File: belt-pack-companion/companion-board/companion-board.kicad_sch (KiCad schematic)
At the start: 4 parts, among them J1 Conn_01x18_Socket, J2 Conn_01x18_Socket, J3 AudioJack4_Ground, U1 TLV320AIC3204

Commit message: companion board update
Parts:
- added D1: Red, PCM_JLCPCB:D_0603, symbol PCM_JLCPCB-Diodes:LED,0603,Red
- added D2: White, PCM_JLCPCB:D_0603, symbol PCM_JLCPCB-Diodes:LED,0603,White
- added D3: Yellow, PCM_JLCPCB:D_0603, symbol PCM_JLCPCB-Diodes:LED,0603,Yellow
- added D4: Green, PCM_JLCPCB:D_0805, symbol PCM_JLCPCB-Diodes:LED,0805,Green
- added J4: Micro_SD_Card, symbol Connector:Micro_SD_Card
- added R1, R2, R3, R4: 27Ω, PCM_JLCPCB:R_0603, symbol PCM_JLCPCB-Resistors:0603,27Ω
- added R5: 10Ω, PCM_JLCPCB:R_0603, symbol PCM_JLCPCB-Resistors:0603,10Ω
- added S1, S2: Tactile Button, 160gf, PCM_JLCPCB:SW_TS-1088-AR02016, symbol PCM_JLCPCB-Connectors_Buttons:Tactile Button, 160gf, 12V, 50mA, 4.0mm
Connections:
- net GND: now reaches J2.1 (Pin_1)
- net GND: now also J1.1 (Pin_1), U1.12 (SPI_SELECT), U1.17 (AVSS), U1.28 (DVSS), U1.33 (EP), U1.7 (IOVSS)
- net +5V: now reaches J2.2 (Pin_2)
- net at U1.1 (MCLK): now also R5.2
- net I^{2}C_SDA: now reaches U1.10 (SDA/MOSI)
- net I^{2}C_SDA: now also J1.16 (Pin_16)
- net at U1.2 (BCLK): now also R3.2
- net at U1.3 (WCLK): now also R4.2
- net at U1.4 (DIN/MFP1): now also R1.2
- net at U1.5 (DOUT/MFP2): now also R2.2
- net I^{2}C_SCL: now reaches U1.9 (SCL/~{SS})
- net I^{2}C_SCL: now also J1.17 (Pin_17)
- net I^{2}S_BCLK: now reaches J1.12 (Pin_12)
- net I^{2}S_BCLK: now also R4.1
- net I^{2}S_WCLK: now reaches J1.13 (Pin_13)
- net I^{2}S_WCLK: now also R3.1
- net I^{2}S_MIC_DATA: now reaches J1.14 (Pin_14)
- net I^{2}S_MIC_DATA: now also R2.1
- net I^{2}S_SPK_DATA: now reaches J1.15 (Pin_15)
- net I^{2}S_SPK_DATA: now also R1.1
- net +3.3V: now reaches J1.2 (Pin_2)
- net +3.3V: now also J1.3 (Pin_3)
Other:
- note added: "Heltec LoRa V3"
- note added: "USB-C"
- moved on the sheet: J1, J2, J3, U1

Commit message: companion-board schematic update
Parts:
- added C1, C4: 10uF, PCM_JLCPCB:C_0402, symbol PCM_JLCPCB-Capacitors:0402,10uF
- added C2: 1uF, PCM_JLCPCB:C_0402, symbol PCM_JLCPCB-Capacitors:0402,1uF
- added C3: 1nF, PCM_JLCPCB:C_0402, symbol PCM_JLCPCB-Capacitors:0402,1nF
- added C5, C6: 47uF, PCM_JLCPCB:C_0805, symbol PCM_JLCPCB-Capacitors:0805,47uF
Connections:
- net +3.3V: now also U1.26 (LDOIN/HPVDD), U1.30 (LDO_SELECT), C1.1, C2.1, C3.1
- net GND: now also J3.G, C1.2, C2.2, C3.2, C4.2
- net at U1.18 (REF): now also C4.1
- net at U1.25 (HPL): now also C5.1
- net at U1.27 (HPR): now also C6.1
- net CODEC_RESET: now reaches U1.31 (~{RESET})
- net CODEC_RESET: now also J1.6 (Pin_6)
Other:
- moved on the sheet: J3, R1, R2, R3, R4, R5, U1

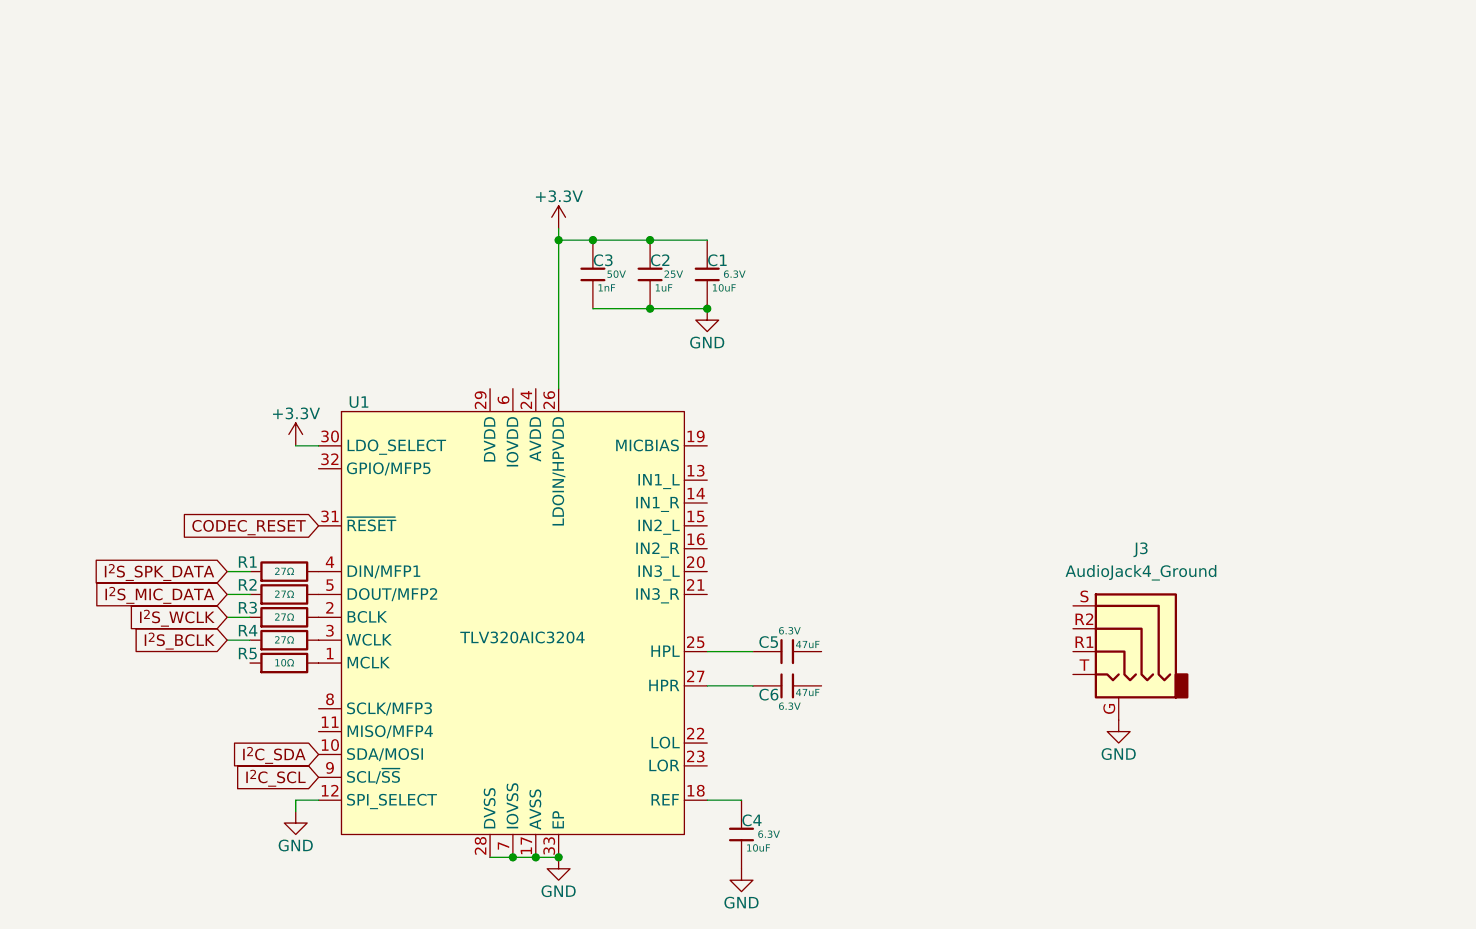
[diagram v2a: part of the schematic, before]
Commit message: Added connections to TRRS jack and some capacitors
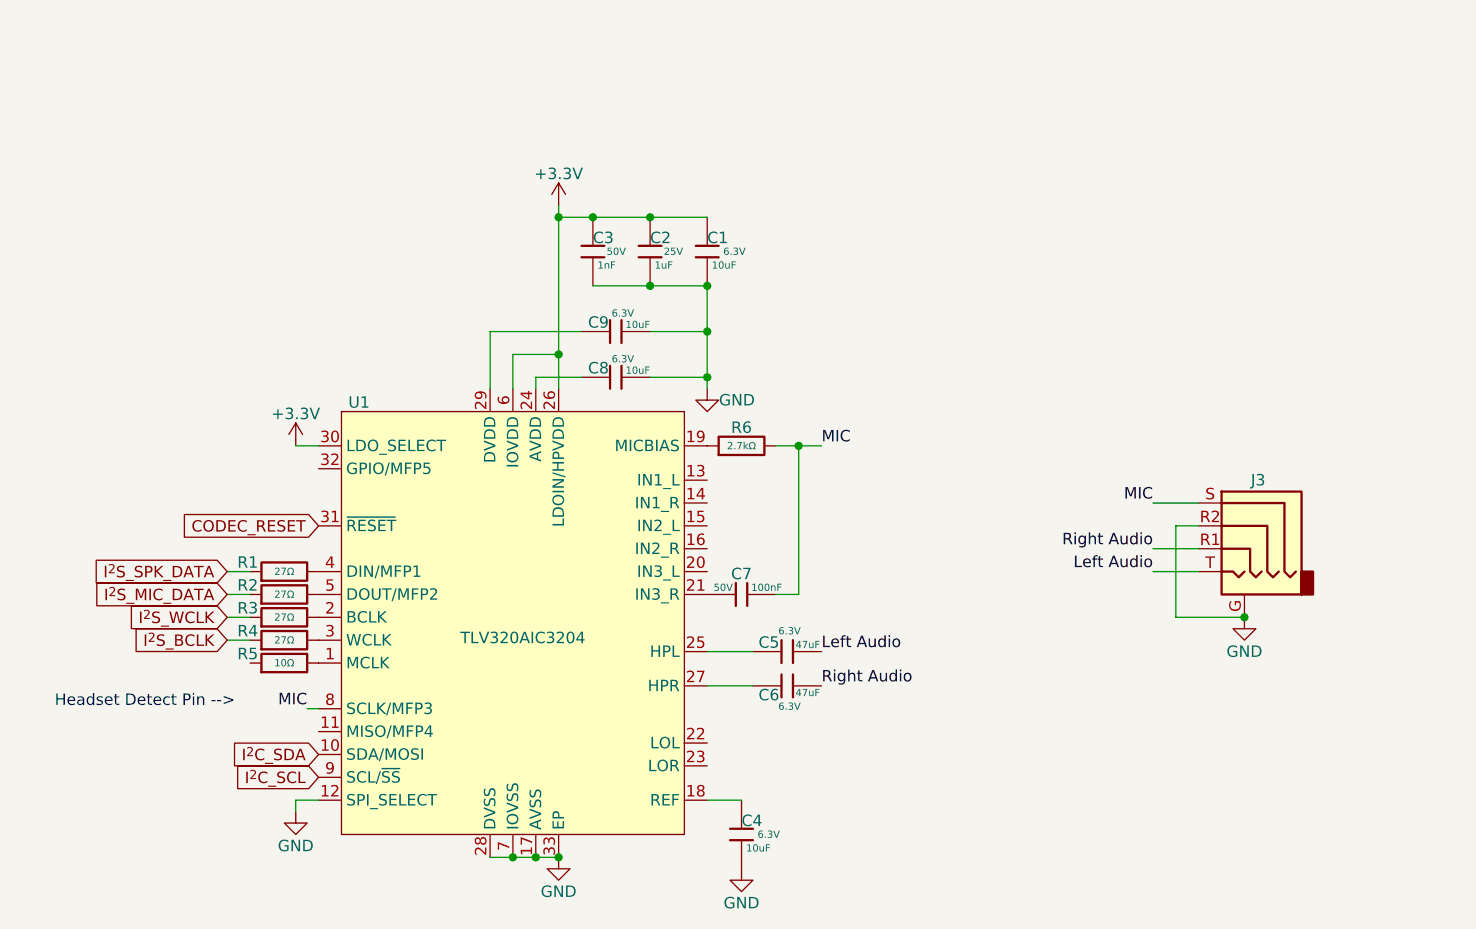
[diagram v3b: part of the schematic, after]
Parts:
- added C7: 100nF, PCM_JLCPCB:C_0603, symbol PCM_JLCPCB-Capacitors:0603,100nF
- added C8, C9: 10uF, PCM_JLCPCB:C_0402, symbol PCM_JLCPCB-Capacitors:0402,10uF
- added R6: 2.7kΩ, PCM_JLCPCB:R_0805, symbol PCM_JLCPCB-Resistors:0805,2.7kΩ
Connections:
- net +3.3V: now also U1.6 (IOVDD)
- net GND: now also J3.R2, C8.2, C9.2
- net Right Audio: now reaches J3.R1
- net Right Audio: now also C6.2
- net MIC: now reaches J3.S
- net MIC: now also U1.8 (SCLK/MFP3), C7.2, R6.2
- net Left Audio: now reaches J3.T
- net Left Audio: now also C5.2
- net at U1.19 (MICBIAS): now also R6.1
- net at U1.21 (IN3_R): now also C7.1
- net at U1.24 (AVDD): now also C8.1
- net at U1.29 (DVDD): now also C9.1
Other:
- note added: "Headset Detect Pin -->"
- moved on the sheet: C1, C2, C3, J3

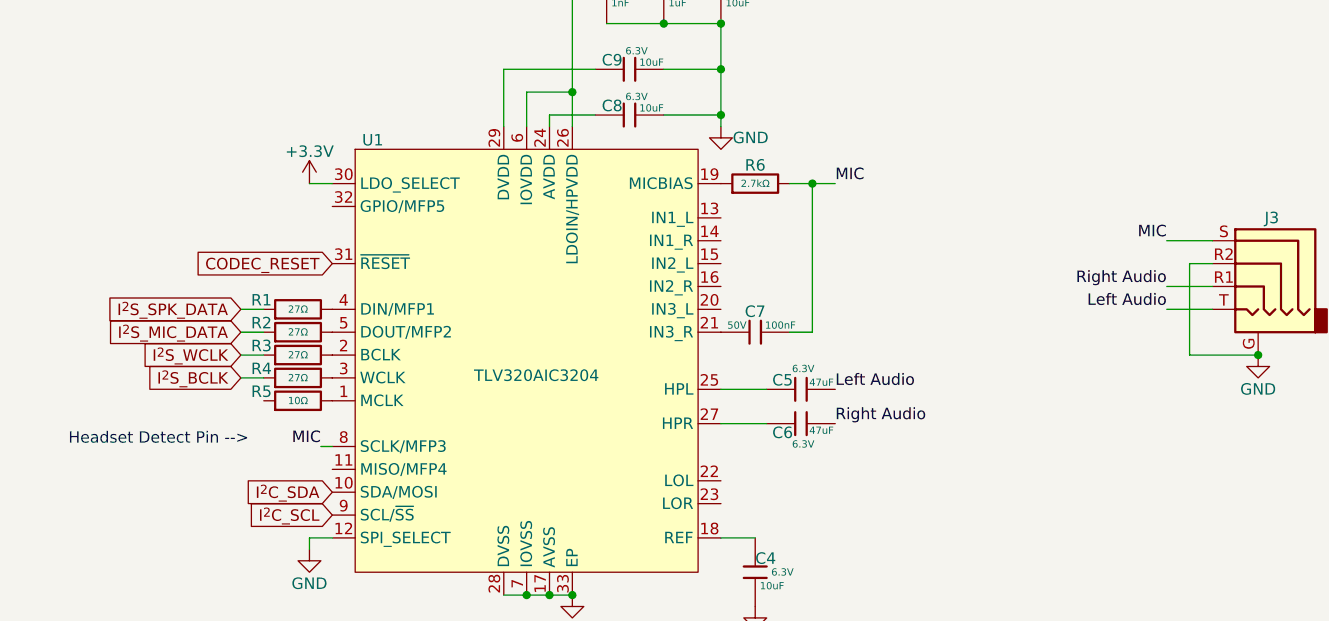
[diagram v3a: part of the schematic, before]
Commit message: Changed labels to global net labels
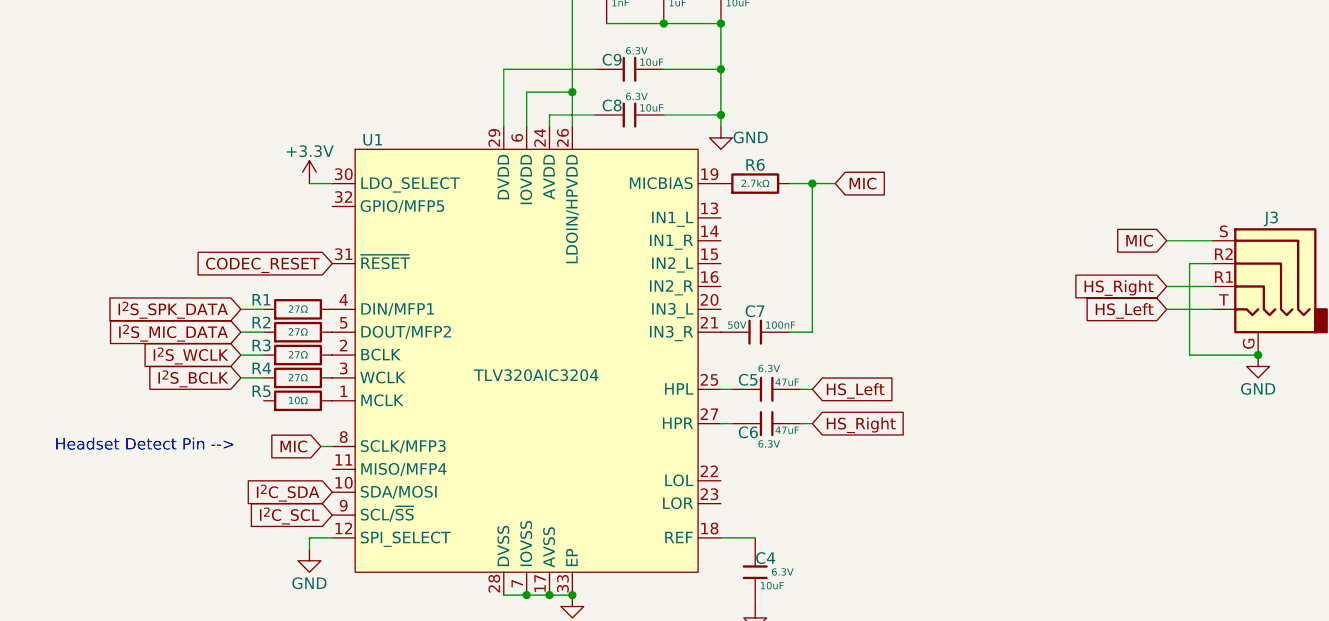
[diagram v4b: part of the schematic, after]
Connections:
- net Left Audio renamed HS_Left
- net Right Audio renamed HS_Right
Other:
- moved on the sheet: C5, C6

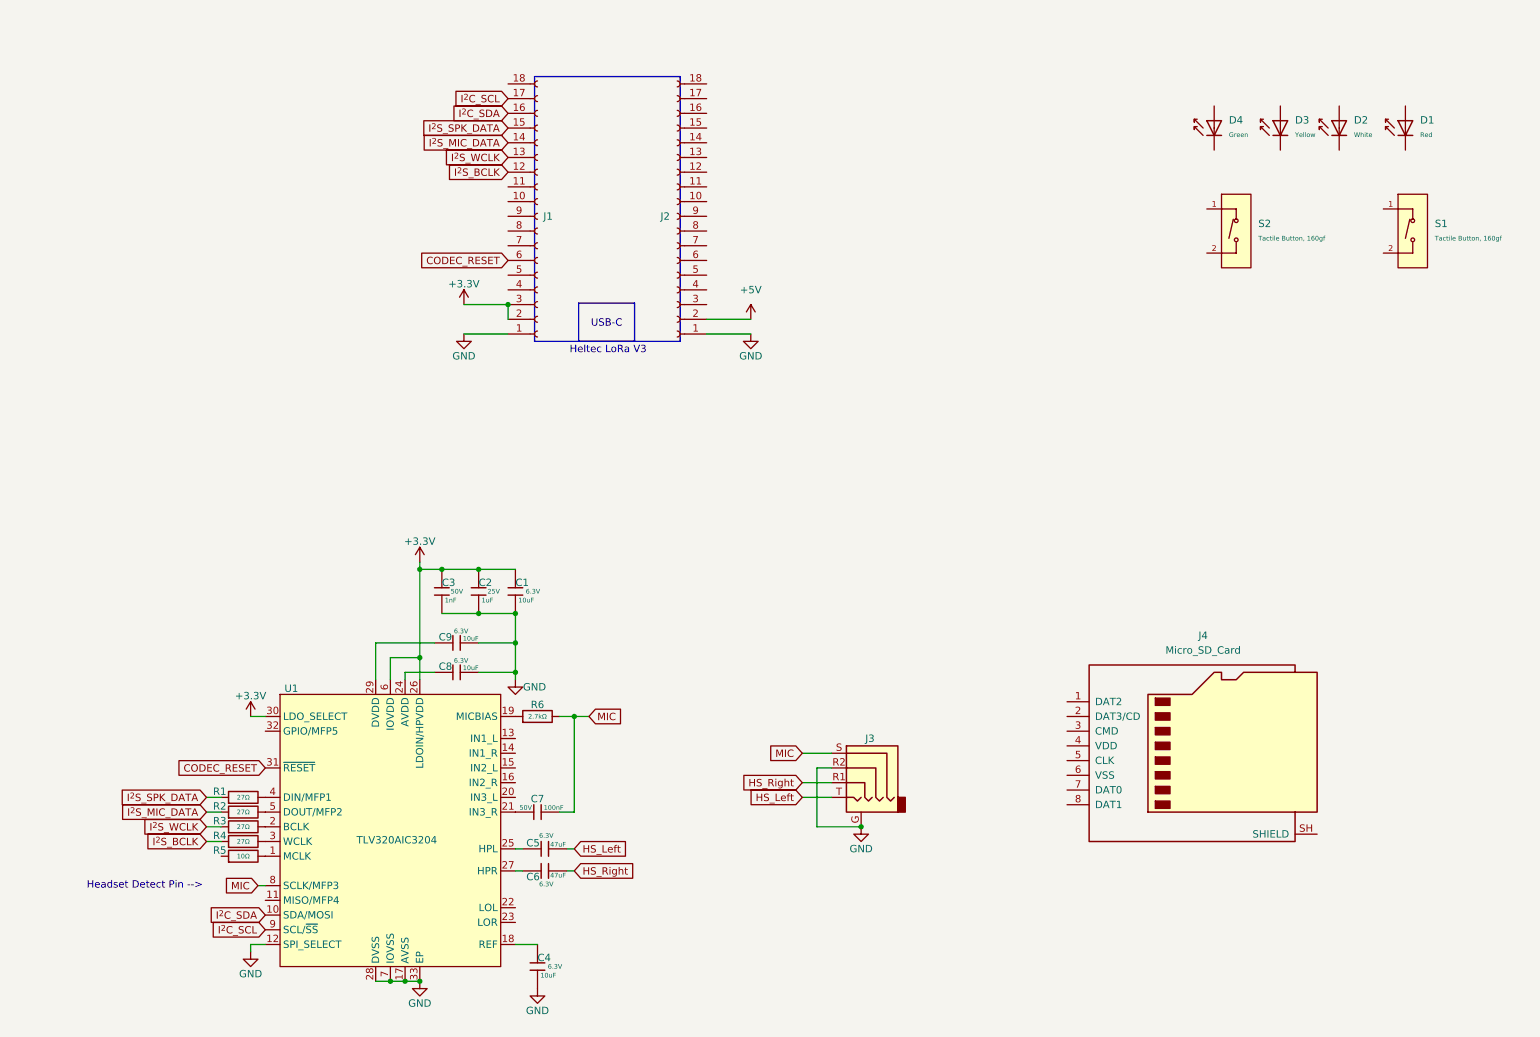
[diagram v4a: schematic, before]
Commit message: Updated pin mapping
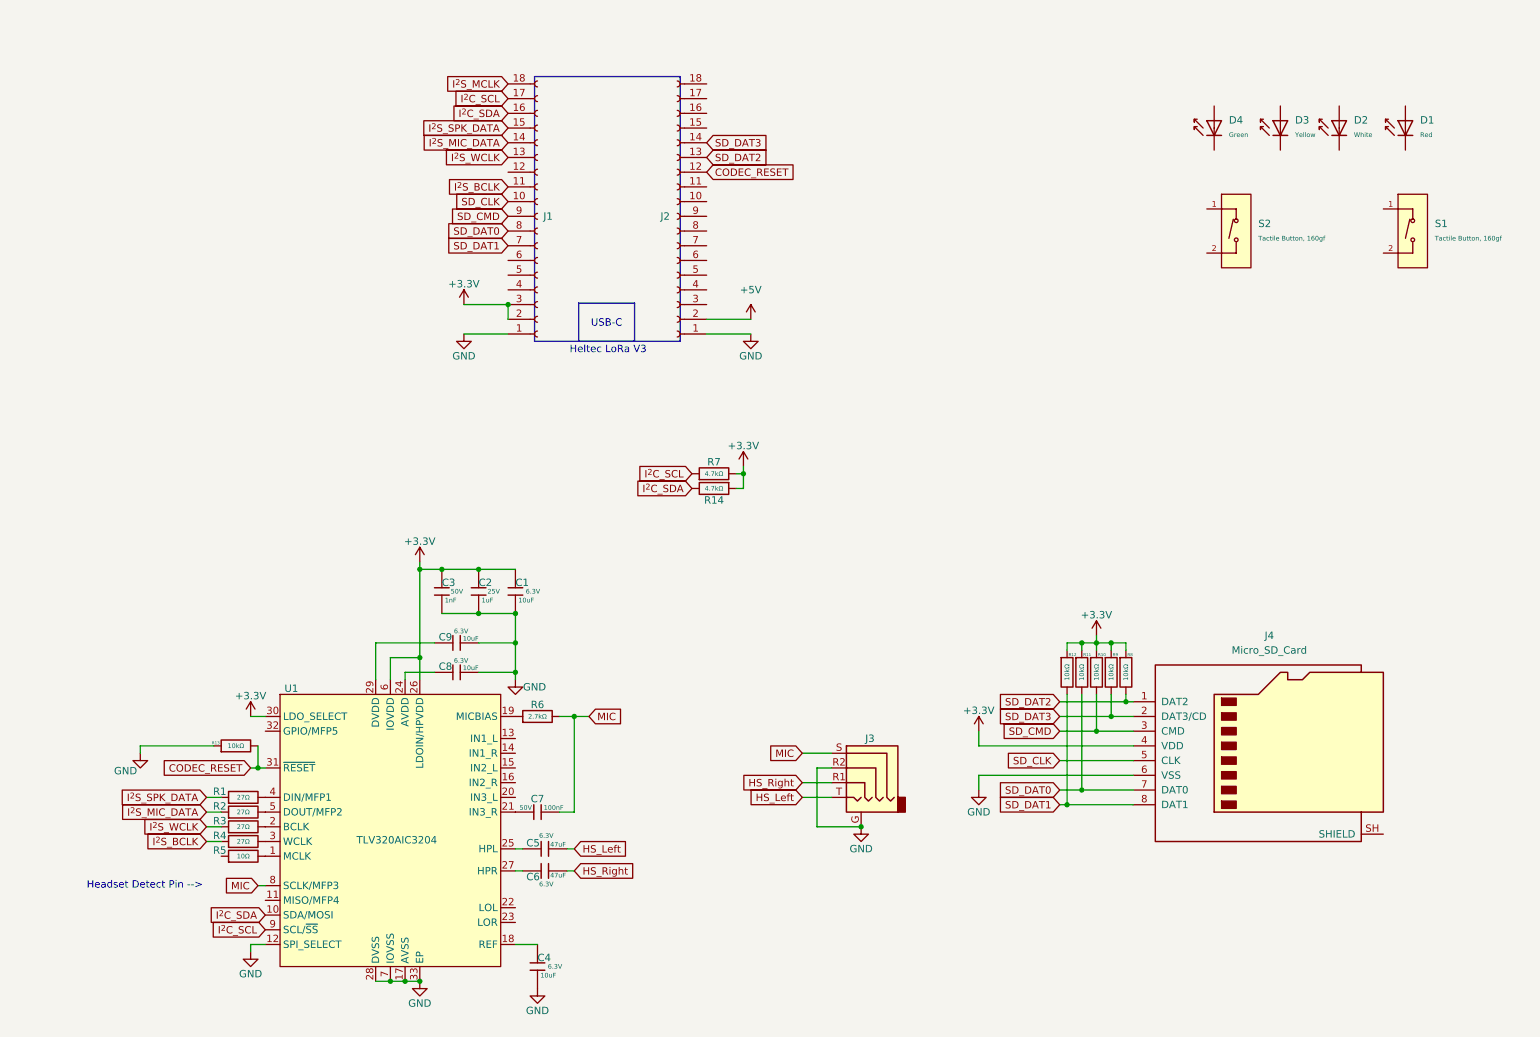
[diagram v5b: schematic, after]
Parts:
- added R10, R11, R12, R13, R8, R9: 10kΩ, PCM_JLCPCB:R_0402, symbol PCM_JLCPCB-Resistors:0402,10kΩ
- added R14, R7: 4.7kΩ, PCM_JLCPCB:R_0402, symbol PCM_JLCPCB-Resistors:0402,4.7kΩ
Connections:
- net +3.3V: now also J4.4 (VDD), R10.1, R11.1, R12.1, R14.1, R7.2, R8.1, R9.1
- net CODEC_RESET: now also J2.12 (Pin_12), R13.2; no longer J1.6 (Pin_6)
- net GND: now also J4.6 (VSS), R13.1
- net I^{2}C_SCL: now also R7.1
- net I^{2}C_SDA: now also R14.2
- net I^{2}S_BCLK: now also J1.11 (Pin_11); no longer J1.12 (Pin_12)
- net SD_DAT2: now reaches J2.13 (Pin_13)
- net SD_DAT2: now also J4.1 (DAT2), R8.2
- net SD_DAT3: now reaches J2.14 (Pin_14)
- net SD_DAT3: now also J4.2 (DAT3/CD), R9.2
- net SD_CMD: now reaches J4.3 (CMD)
- net SD_CMD: now also J1.9 (Pin_9), R10.2
- net SD_CLK: now reaches J4.5 (CLK)
- net SD_CLK: now also J1.10 (Pin_10)
- net SD_DAT0: now reaches J4.7 (DAT0)
- net SD_DAT0: now also J1.8 (Pin_8), R11.2
- net SD_DAT1: now reaches J4.8 (DAT1)
- net SD_DAT1: now also J1.7 (Pin_7), R12.2
- net I^{2}S_MCLK: now reaches J1.18 (Pin_18)
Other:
- moved on the sheet: J4
